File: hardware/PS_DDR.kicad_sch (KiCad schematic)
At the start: 38 parts, among them U1 DDR3, U2 xc7z020clg400

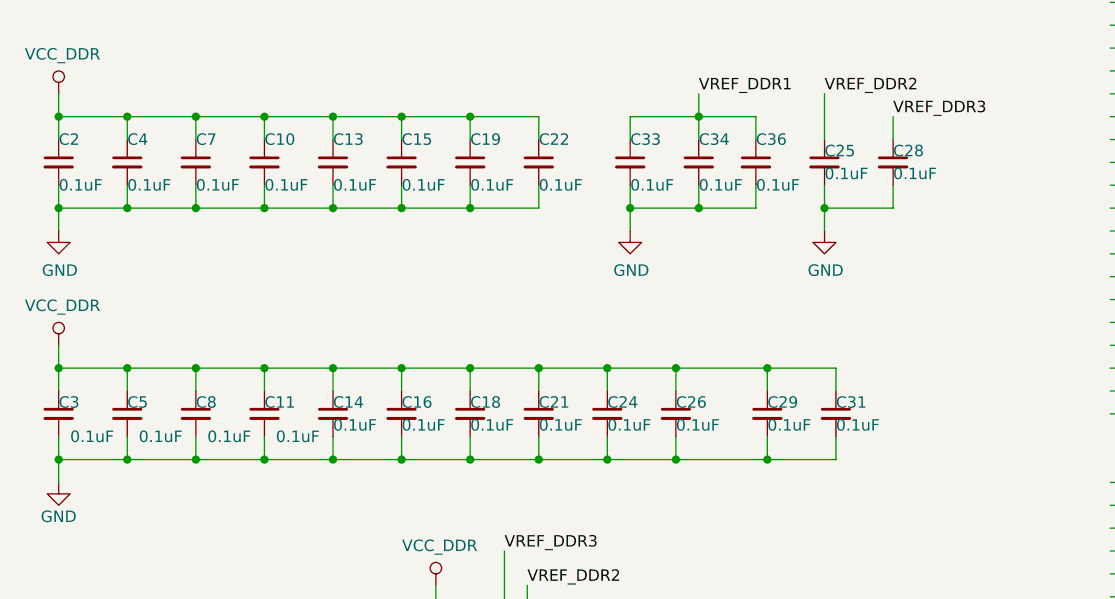
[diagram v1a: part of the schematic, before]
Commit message: Modify wrong DCDC TPS62088 package Panelize PCB Add manufacture requirements files
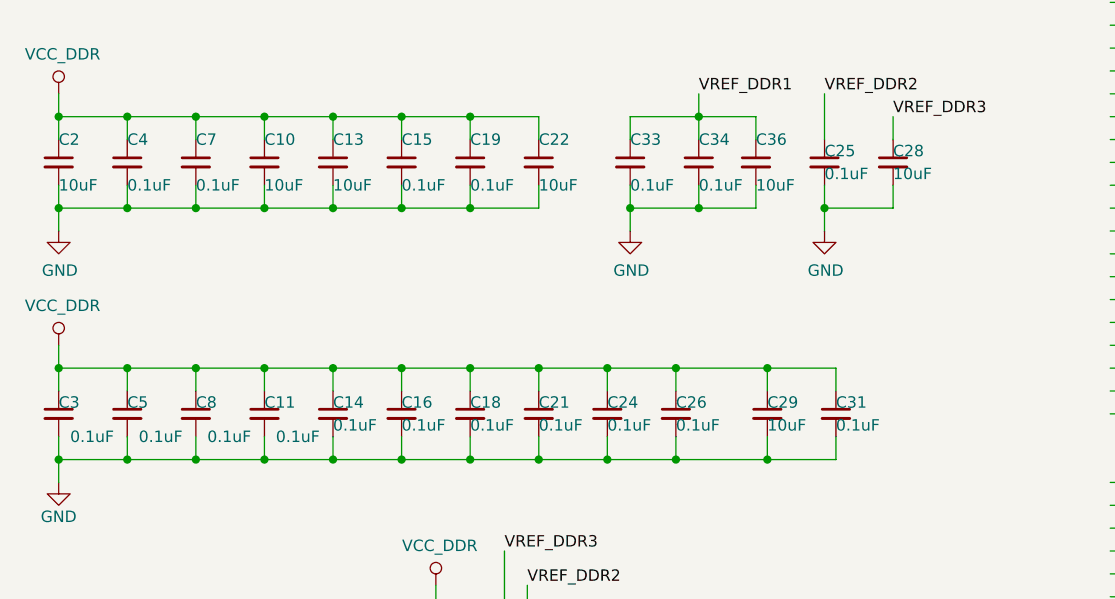
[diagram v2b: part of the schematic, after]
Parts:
- C10, C13, C2, C22, C28, C29, C36: value 0.1uF -> 10uF
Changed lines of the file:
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@@
       (effects (font (size 1.27 1.27)) (justify left))
     )
-    (property "Value" "0.1uF" (id 1) (at 208.28 82.55 0)
+    (property "Value" "10uF" (id 1) (at 208.28 82.55 0)
       (effects (font (size 1.27 1.27)) (justify left))
     )
@@
       (effects (font (size 1.27 1.27)) (justify left))
     )
-    (property "Value" "0.1uF" (id 1) (at 138.43 83.82 0)
+    (property "Value" "10uF" (id 1) (at 138.43 83.82 0)
       (effects (font (size 1.27 1.27)) (justify left))
     )
@@
       (effects (font (size 1.27 1.27)) (justify left))
     )
-    (property "Value" "0.1uF" (id 1) (at 193.04 83.82 0)
+    (property "Value" "10uF" (id 1) (at 193.04 83.82 0)
       (effects (font (size 1.27 1.27)) (justify left))
     )
@@
       (effects (font (size 1.27 1.27)) (justify left))
     )
-    (property "Value" "0.1uF" (id 1) (at 115.57 83.82 0)
+    (property "Value" "10uF" (id 1) (at 115.57 83.82 0)
       (effects (font (size 1.27 1.27)) (justify left))
     )
@@
       (effects (font (size 1.27 1.27)) (justify left))
     )
-    (property "Value" "0.1uF" (id 1) (at 168.91 83.82 0)
+    (property "Value" "10uF" (id 1) (at 168.91 83.82 0)
       (effects (font (size 1.27 1.27)) (justify left))
     )
@@
       (effects (font (size 1.27 1.27)) (justify left))
     )
-    (property "Value" "0.1uF" (id 1) (at 194.31 110.49 0)
+    (property "Value" "10uF" (id 1) (at 194.31 110.49 0)
       (effects (font (size 1.27 1.27)) (justify left))
     )
@@
       (effects (font (size 1.27 1.27)) (justify left))
     )
-    (property "Value" "0.1uF" (id 1) (at 146.05 83.82 0)
-      (effects (font (size 1.27 1.27)) (justify left))
-    )
+    (property "Value" "10uF" (id 1) (at 146.05 83.82 0)
+      (effects (font (size 1.27 1.27)) (justify left))
+    )
